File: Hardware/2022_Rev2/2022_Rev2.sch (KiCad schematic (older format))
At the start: 19 parts, among them U1 OKI-78SR-5_1.5-W36-C

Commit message: Fixed many issues
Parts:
- removed C1: 22uF, Capacitor_THT:CP_Radial_D6.3mm_P2.50mm, symbol Device:CP1
- removed C3: 47uF, Capacitor_THT:CP_Radial_D6.3mm_P2.50mm, symbol Device:CP1
- removed unit 1 of Conn4
- removed U1: OKI-78SR-5_1.5-W36-C, Converter_DCDC:Converter_DCDC_muRata_OKI-78SR_Vertical, symbol Converter_DCDC:OKI-78SR-5_1.5-W36-C
- added C1: 10uF, Capacitor_SMD:C_0603_1608Metric_Pad1.08x0.95mm_HandSolder, symbol Device:C
- added C3, C4, C5, C6: 10 uF, symbol Device:C_Small
- added Conn1: AndersonPP, MRDT_Connectors:Anderson_2_Vertical_Side_by_Side_PV, symbol 2022_Rev2-rescue:AndersonPP-MRDT_Connectors
- added unit 3 of Conn4
- added D2: LED, Diode_SMD:D_0603_1608Metric_Pad1.05x0.95mm_HandSolder, symbol Device:D
- added R2: 0.0025, Resistor_SMD:R_2512_6332Metric_Pad1.40x3.35mm_HandSolder, symbol Device:R
- added R3: 1k, Resistor_SMD:R_0603_1608Metric_Pad0.98x0.95mm_HandSolder, symbol Device:R
- added U1: TSR1-2433, symbol MRDT_Devices:TSR1-2433
- added U2: INA281, Package_TO_SOT_SMD:SOT-23-5, symbol 2022_Rev2-rescue:INA281-MRDT_ICs
- added VR1, VR2: Q36SR12020NRFA, symbol MRDT_Devices:Q36SR12020NRFA
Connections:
- net Driver_NetSwitch is gone; now on net Driver_Spare: Conn19.10
- net +5V: now also U1.3 (Vout), U2.5 (V+)
- net Current_Sense_AuxAct: now also U2.1
- net Current_Sense_NetSwitch: no longer Conn18.10
- net Current_Sense_Spare: now also Conn18.10
- net Driver_AuxAct: now also VR1.6 (TRIM)
- net GND: now also C1.2, C3.1, C4.1, C5.2, C6.2, Conn1.1 (GND), D2.1 (K), U1.2 (GND), U2.2 (GND), VR1.2 (REMOTE), VR1.3 (-VIN), VR1.4 (-VOUT), VR1.5 (SENSE(-)), VR2.2 (REMOTE), VR2.3 (-VIN), VR2.4 (-VOUT), VR2.5 (SENSE(-))
- net 12V/Anderson_AuxLog: no longer names the net of Conn4.2 (V+Log)
- net 12V/Anderson_AuxLog: now also Conn4.3 (V+Act), R2.2, U2.4 (-)
- net PV renamed +36V
- net +36V: now also C3.2, C4.2, VR1.1 (+VIN), VR2.1 (+VIN)
- new net: D2.2 (A), R3.1
- new net: C5.1, R2.1, R3.2, U2.3 (+), VR1.7 (SENSE(+)), VR1.8 (+VOUT)
- new net +12VA: C1.1, C6.1, U1.1 (Vin), VR2.7 (SENSE(+)), VR2.8 (+VOUT)
- no-connect marks 0 -> 1
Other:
- moved on the sheet: Conn4B

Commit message: ahhhhhh ladybug is angy
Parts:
- C3, C4, C5, C6: footprint (none) -> Capacitor_SMD:C_0603_1608Metric_Pad1.05x0.95mm_HandSolder
- Conn10: value AndersonPP -> Nav
- Conn11: value AndersonPP -> Network Switch
- Conn12: value AndersonPP -> Multimedia
- Conn2: value AndersonPP -> Pack
- Conn3: value AndersonPP -> Spare
- Conn4: renamed from Conn1; value AndersonPP -> Aux; footprint MRDT_Connectors:Anderson_2_Vertical_Side_by_Side_PV -> MRDT_Connectors:Anderson_3_Vertical_Side_by_Side
- Conn4: value AndersonPP -> Aux; footprint MRDT_Connectors:Anderson_2_Vertical_Sidy_by_Side -> MRDT_Connectors:Anderson_3_Vertical_Side_by_Side
- Conn5: value AndersonPP -> BBB
- Conn6: value AndersonPP -> Cam1
- Conn7: value AndersonPP -> Cam2
- Conn8: value AndersonPP -> Drive
- Conn9: value AndersonPP -> Gimbal
- R2: value 0.0025 -> 0.003; footprint Resistor_SMD:R_2512_6332Metric_Pad1.40x3.35mm_HandSolder -> Resistor_SMD:R_2010_5025Metric_Pad1.52x2.65mm_HandSolder
- U1: footprint (none) -> MRDT_Devices:TSR_1-2433
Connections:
- net GND: no longer VR1.2 (REMOTE)
- removed net 12V/Anderson_Spare_Act: Conn3.3 (V+Act)
- net Current_Sense_AuxAct renamed Current_Sense_Aux
- net Current_Sense_AuxLog: no longer names the net of Conn18.1
- net Driver_AuxAct: no longer names the net of VR1.6 (TRIM)
- net Driver_AuxAct: no longer Conn19.2
- net Driver_AuxLog: no longer names the net of Conn19.1
- new net 12V/Anderson_Spare: Conn3.2 (V+Log)
- new net Driver_Aux: Conn19.2, VR1.2 (REMOTE)
- no-connect marks 1 -> 4

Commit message: Gerbs are done
please review before you order this max
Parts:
- removed C3, C4, C5, C6: 10 uF, Capacitor_SMD:C_0603_1608Metric_Pad1.05x0.95mm_HandSolder, symbol Device:C_Small
- removed Conn18, Conn19: Molex_SL_10, MRDT_Connectors:MOLEX_SL_10_Vertical, symbol MRDT_Connectors:Molex_SL_10
- added Conn1, Conn13: Molex_SL_09, MRDT_Connectors:MOLEX_SL_09_Horizontal, symbol MRDT_Connectors:Molex_SL_09
- added unit 3 of Conn3
- C1: footprint Capacitor_SMD:C_0603_1608Metric_Pad1.08x0.95mm_HandSolder -> Capacitor_SMD:C_0603_1608Metric_Pad1.05x0.95mm_HandSolder
- C2: value 10uF -> 22uF; footprint Capacitor_SMD:C_0603_1608Metric_Pad1.08x0.95mm_HandSolder -> Capacitor_SMD:C_0603_1608Metric_Pad1.05x0.95mm_HandSolder
- Conn10, Conn11, Conn5, Conn6, Conn7, Conn8: footprint MRDT_Connectors:Anderson_2_Vertical_Sidy_by_Side -> MRDT_Connectors:Square_Anderson_2_H_Stacked_PV
- Conn12, Conn3: footprint MRDT_Connectors:Anderson_2_Vertical_Sidy_by_Side -> MRDT_Connectors:Square_Anderson_3_H_Side_By_Side
- Conn2: footprint MRDT_Connectors:Anderson_2_Vertical_Side_by_Side_PV -> MRDT_Connectors:Square_Anderson_2_H_Stacked
- Conn4, Conn9: footprint MRDT_Connectors:Anderson_3_Vertical_Side_by_Side -> MRDT_Connectors:Square_Anderson_3_H_Side_By_Side
- R1, R3: footprint Resistor_SMD:R_0603_1608Metric_Pad0.98x0.95mm_HandSolder -> Resistor_SMD:R_0603_1608Metric_Pad1.05x0.95mm_HandSolder
- R2: value 0.003 -> 0.0015; footprint Resistor_SMD:R_2010_5025Metric_Pad1.52x2.65mm_HandSolder -> Resistor_SMD:R_2512_6332Metric_Pad1.52x3.35mm_HandSolder
- VR1, VR2: footprint (none) -> MRDT_Devices:Q36SR12020NRFA
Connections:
- net 12V/Anderson_Cam1: now also Conn6.2 (V+Log); no longer Conn6.3 (V+Act)
- net 12V/Anderson_Cam2: now also Conn7.2 (V+Log); no longer Conn7.3 (V+Act)
- net 12V/Anderson_NetSwitch: now also Conn11.2 (V+Log); no longer Conn11.3 (V+Act)
- net 12V/Anderson_Spare: now also Conn3.3 (V+Act)
- net Current_Sense_Aux: now also Conn1.1
- net Current_Sense_BBB: now also Conn1.2
- net Current_Sense_Cam1: now also Conn1.3
- net Current_Sense_Cam2: now also Conn1.4
- net Current_Sense_Drive: now also Conn1.5
- net Current_Sense_Gim: now also Conn1.6
- net Current_Sense_Multi: now also Conn1.7
- net Current_Sense_Nav: now also Conn1.8
- net Current_Sense_Spare: now also Conn1.9
- net Driver_Aux: now also Conn13.9
- net Driver_BBB: now also Conn13.8
- net Driver_Cam1: now also Conn13.7
- net Driver_Cam2: now also Conn13.6
- net Driver_Drive: now also Conn13.5
- net Driver_Gim: now also Conn13.4
- net Driver_Multi: now also Conn13.3
- net Driver_Nav: now also Conn13.2
- net Driver_Spare: now also Conn13.1
- no-connect marks 4 -> 2

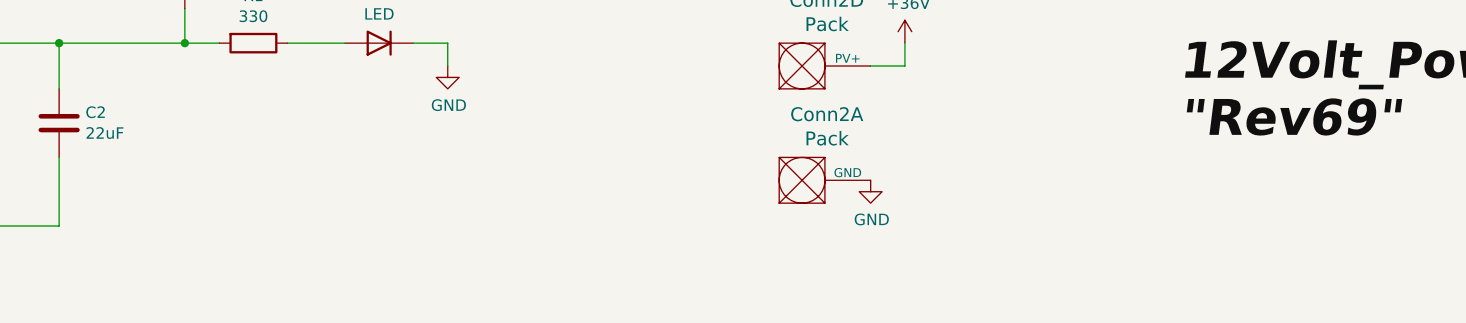
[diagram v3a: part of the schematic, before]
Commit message: made a comment about the current sensor
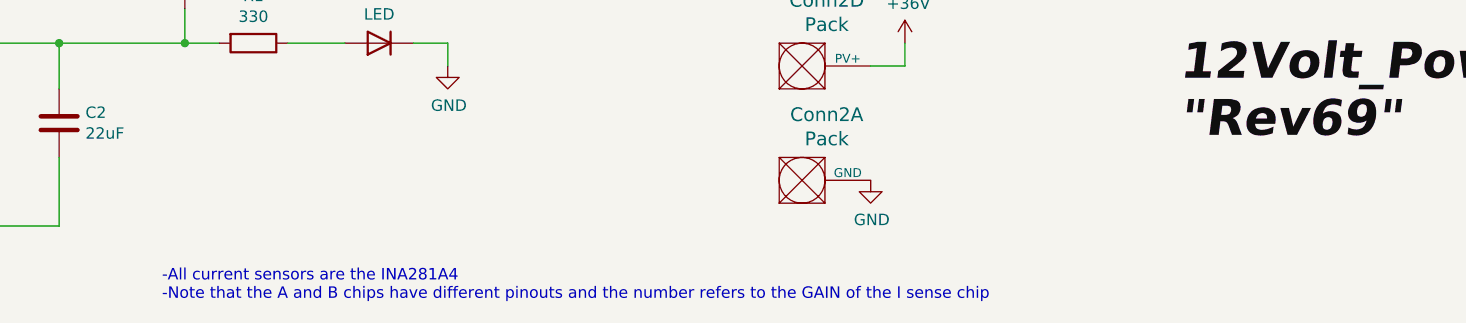
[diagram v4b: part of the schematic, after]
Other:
- note added: "-All current sensors are the INA281A4\n-Note that the A and B chips have different pinouts and the number refers to the GAIN of the I sense chip"
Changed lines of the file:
@@
 	-1   0    0    1
 $EndComp
+Text Notes 2650 7730 0    50   ~ 0
+-All current sensors are the INA281A4\n-Note that the A and B chips have different pinouts and the number refers to the GAIN of the I sense chip
 $EndSCHEMATC
